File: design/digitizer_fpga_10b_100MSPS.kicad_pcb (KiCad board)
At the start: 4 copper layers, 125 x 60 mm, 284 parts, among them J1 POWER, J2 SWD_01X04, J3 DEBUG_SPI, J4 USB_B_Mini, J5 SMA, J6 JUMPER_DFS/GAIN, J7 DEBUG_FPGA_GPIO, J8 DIGILENT_JTAG_HS2_01X06, SW1 RST, SW2 PROG, U1 LM3880MF-1AA, U10 IS61WV12816EDBLL-10TLI, U11 TLV431ACDBZR, U12 AD9214, U13 XC7S15-FTGB196, U14 IS25LP064A-JKx, U2 NCP59744MN1, U3 NCP59744MN1, U4 NCP59744MN1, U5 NCP59744MN1, U6 STM32H750VBTx, U7 USBLC6-2SC6, U8 FT231XS, U9 ADA4930-1, X1 ASTX-H11-25.000MHZ-T

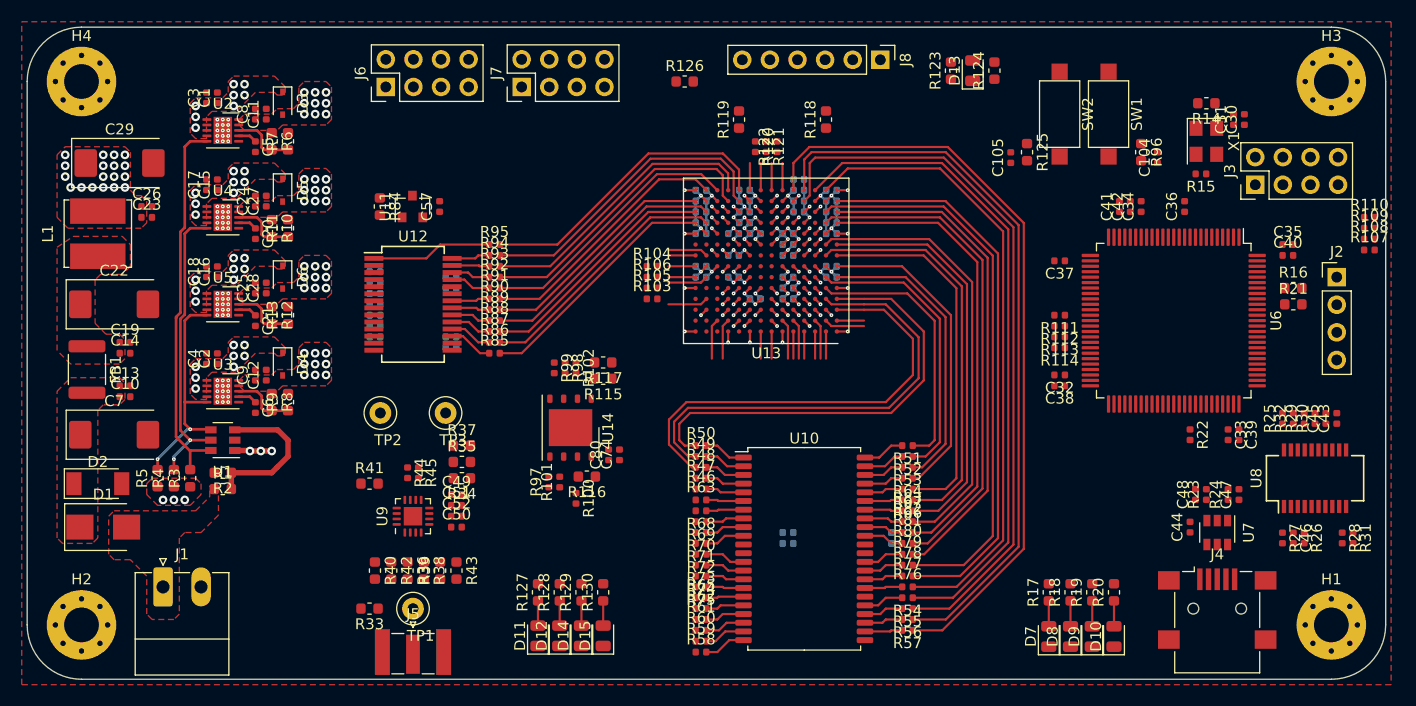
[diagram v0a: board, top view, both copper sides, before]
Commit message: Updated ADC layout
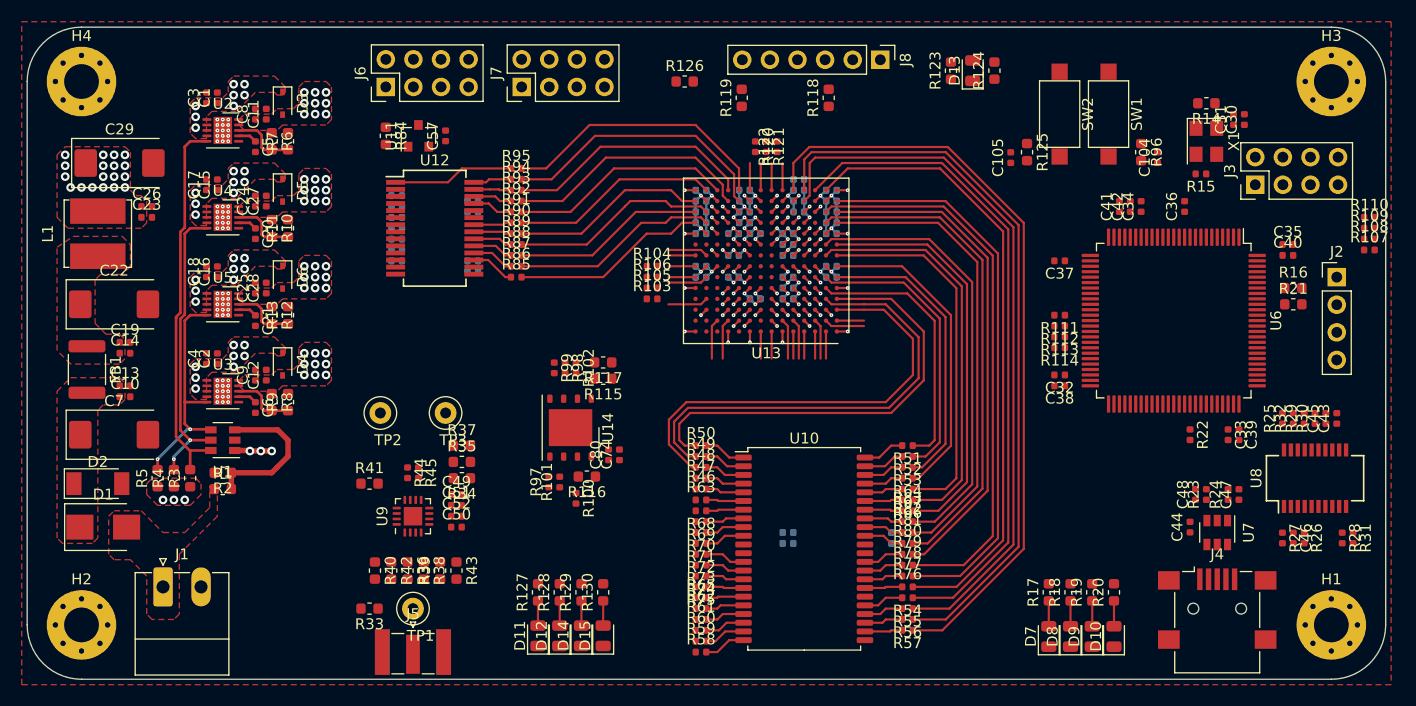
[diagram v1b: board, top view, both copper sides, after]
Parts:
- moved C58 7.28 mm to (104.0, 105.5)
- moved C59 7.28 mm to (104.0, 109.5)
- moved C60 7.28 mm to (104.0, 106.5)
- moved C61 7.28 mm to (104.0, 110.5)
- moved C62 7.28 mm to (111.0, 111.5)
- moved C63 7.28 mm to (104.0, 111.5)
- moved C64 7.28 mm to (111.0, 106.0)
- moved C65 7.28 mm to (111.0, 112.5)
- moved C66 7.28 mm to (104.0, 107.5)
- moved C67 7.28 mm to (111.0, 107.0)
- moved C68 7.28 mm to (104.0, 108.5)
- moved R85 7.28 mm to (115.0, 113.0)
- moved R86 7.28 mm to (115.0, 112.0)
- moved R87 7.28 mm to (115.0, 111.0)
- moved R88 7.28 mm to (115.0, 110.0)
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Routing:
- net /ADC_DATA5: track 24.0 -> 19.1 mm
- net /ADC_DATA2: track 22.6 -> 17.7 mm
- net /ADC_DATA1: track 24.0 -> 19.1 mm
- net /ADC_DATA0: track 23.0 -> 18.1 mm
- net /ADC_DATA7: track 27.5 -> 22.9 mm
- net /ADC_DATA3: track 23.6 -> 19.1 mm
- net /ADC_DATA6: track 25.0 -> 20.5 mm
- net /ADC_DATA4: track 22.2 -> 18.1 mm
- net /ADC_DATA8: track 26.8 -> 22.9 mm
- net /ADC_DATA9: track 28.6 -> 25.3 mm
- net /ADC_OVRNG: track 28.0 -> 25.3 mm
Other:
- net class Default: clearance 0.125 -> 0.15
- rule trace_clearance: 0.125 -> 0.15

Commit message: Added some tracks
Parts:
- moved R100 13.8 mm to (125.5, 120.5), turned to 0 degrees
- moved C74 13.2 mm to (121.5, 116.5), turned to 180 degrees
- moved C80 12.0 mm to (121.5, 117.5), turned to 180 degrees
- moved R116 12.0 mm to (123.5, 119.5), turned to -90 degrees
- moved R101 11.0 mm to (124.0, 122.0), turned to 180 degrees
- moved R97 10.7 mm to (124.0, 123.0), turned to 180 degrees
- moved R117 10.4 mm to (113.0, 118.0), turned to -90 degrees
- moved R115 9.55 mm to (114.5, 118.0), turned to -90 degrees
- moved R102 7.05 mm to (113.5, 120.5), turned to 0 degrees
- moved R98 6.00 mm to (113.5, 121.5), turned to 0 degrees
- moved U14 5.93 mm to (119.0, 121.0), turned to 0 degrees
- moved R99 5.13 mm to (113.5, 122.5), turned to 0 degrees
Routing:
- net /MCU/DEBUG_LED1: track 0.00 -> 20.5 mm
- net /MCU/DEBUG_LED2: track 0.00 -> 19.9 mm
- net /MCU/DEBUG_LED3: track 0.00 -> 19.2 mm
- net /MCU/DEBUG_LED4: track 0.00 -> 18.6 mm

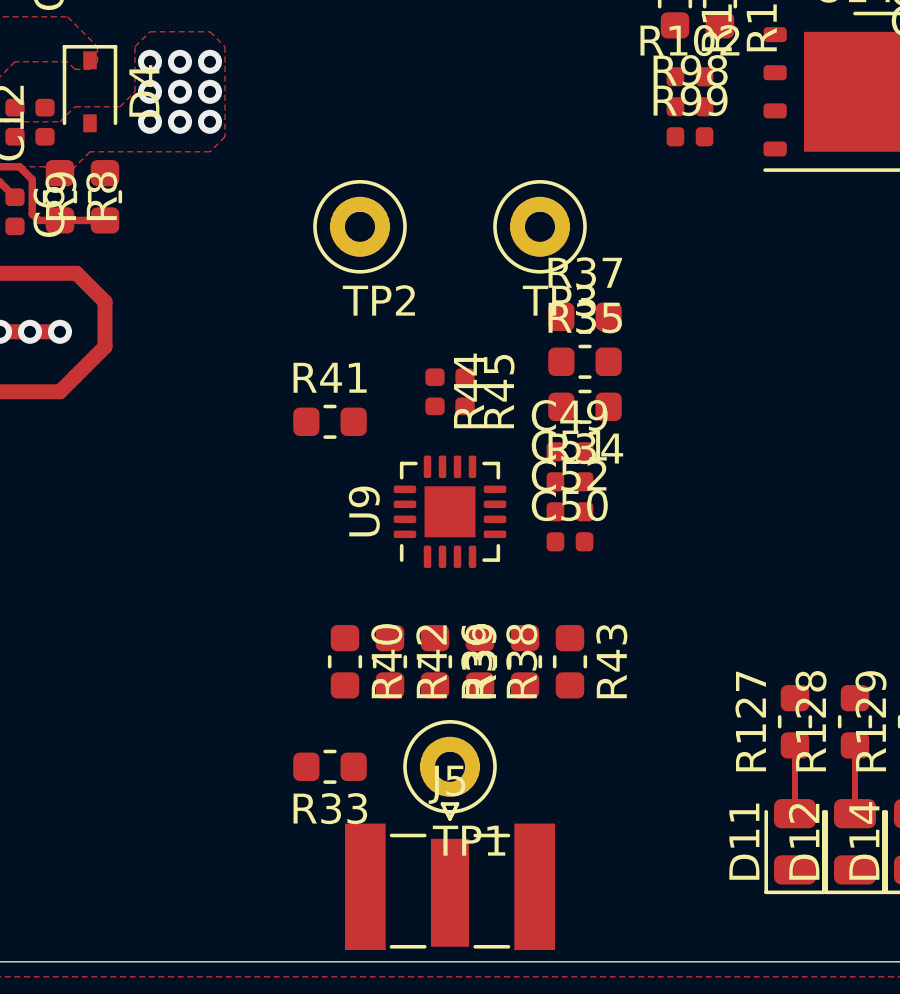
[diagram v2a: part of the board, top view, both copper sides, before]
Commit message: Changed TP footprint
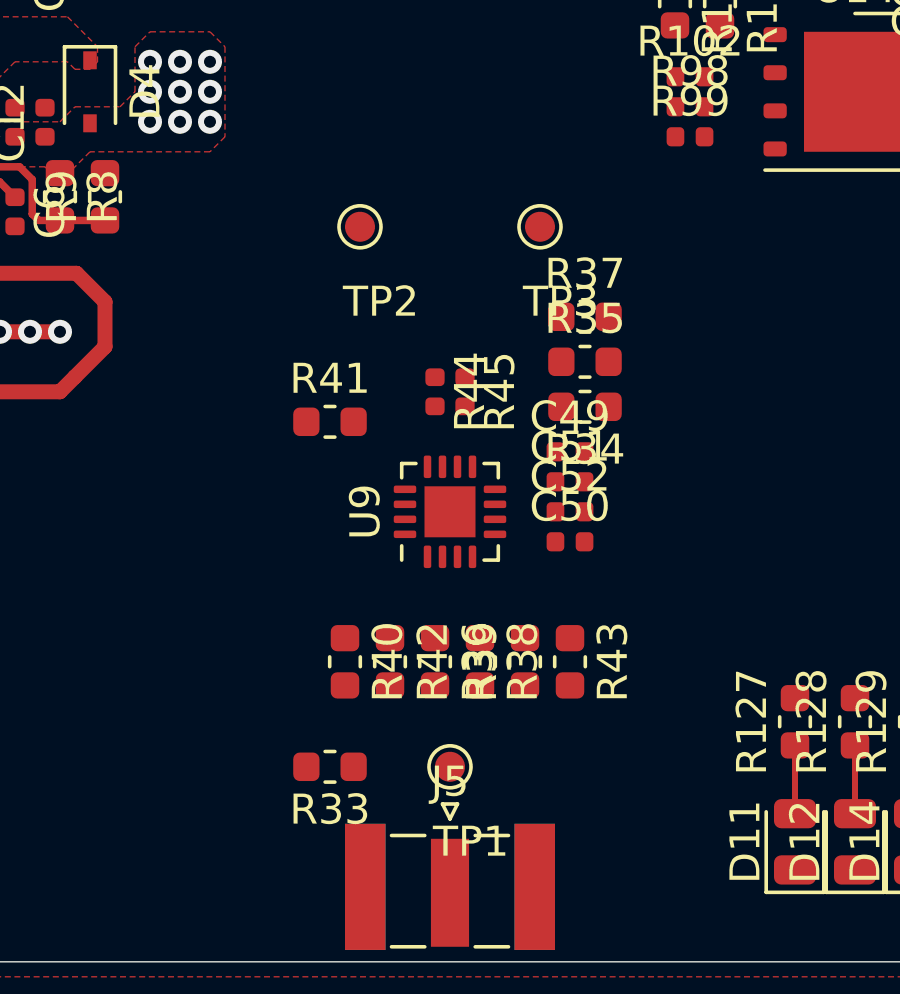
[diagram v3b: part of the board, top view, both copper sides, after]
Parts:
- TP1, TP2, TP3: footprint TestPoint:TestPoint_Loop_D2.50mm_Drill1.0mm_LowProfile -> TestPoint:TestPoint_Pad_D1.0mm
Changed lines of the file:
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@@
-(kicad_pcb (version 20200119) (host pcbnew "5.99.0-unknown-acdfeee~101~ubuntu18.04.1")
+(kicad_pcb (version 20200119) (host pcbnew "5.99.0-unknown-9ca61b5~101~ubuntu18.04.1")
   (general
     (thickness 1.628)
@@
       (dielectric_constraints yes)
     )
-    (last_trace_width 0.2)
+    (last_trace_width 0.25)
     (user_trace_width 0.2)
     (user_trace_width 0.5)
@@
     (add_net "Net-(U8-Pad8)")
   )
+  (module "TestPoint:TestPoint_Pad_D1.0mm" (layer "TOP")
+    (at 105.5 143.5)
+    (descr "SMD pad as test Point, diameter 1.0mm")
+    (tags "test point SMD pad")
+    (attr virtual)
+    (fp_text reference "TP1" (at 0.7 2.5) (layer "F.SilkS")
+      (effects (font (size 1 1) (thickness 0.15)))
+    )
+    (fp_text value "TestPoint_Probe" (at 0 -2.8) (layer "F.Fab")
+      (effects (font (size 1 1) (thickness 0.15)))
+    )
+    (fp_circle (center 0 0) (end 0 0.7) (layer "F.SilkS") (width 0.12))
+    (fp_circle (center 0 0) (end 1 0) (layer "F.CrtYd") (width 0.05))
+    (fp_text user "${REFERENCE}" (at 0.7 2.5) (layer "F.Fab")
+      (effects (font (size 1 1) (thickness 0.15)))
+    )
+    (pad "1" smd circle (at 0 0) (size 1 1) (layers "TOP" "F.Mask")
+      (net 19 "/LNA/IN") (pinfunction "1"))
+    (model "${KISYS3DMOD}/TestPoint.3dshapes/TestPoint_Loop_D2.50mm_Drill1.0mm_LowProfile.wrl"
+      (at (xyz 0 0 0))
+      (scale (xyz 1 1 1))
+      (rotate (xyz 0 0 0))
+    )
+  )
+  (module "TestPoint:TestPoint_Pad_D1.0mm" (layer "TOP")
+    (at 108.5 125.5)
+    (descr "SMD pad as test Point, diameter 1.0mm")
+    (tags "test point SMD pad")
+    (attr virtual)
+    (fp_text reference "TP3" (at 0.7 2.5) (layer "F.SilkS")
+      (effects (font (size 1 1) (thickness 0.15)))
+    )
+    (fp_text value "TestPoint_Probe" (at 0 -2.8) (layer "F.Fab")
+      (effects (font (size 1 1) (thickness 0.15)))
+    )
+    (fp_circle (center 0 0) (end 0 0.7) (layer "F.SilkS") (width 0.12))
+    (fp_circle (center 0 0) (end 1 0) (layer "F.CrtYd") (width 0.05))
+    (fp_text user "${REFERENCE}" (at 0.7 2.5) (layer "F.Fab")
+      (effects (font (size 1 1) (thickness 0.15)))
+    )
+    (pad "1" smd circle (at 0 0) (size 1 1) (layers "TOP" "F.Mask")
+      (net 39 "/OUT+") (pinfunction "1"))
+    (model "${KISYS3DMOD}/TestPoint.3dshapes/TestPoint_Loop_D2.50mm_Drill1.0mm_LowProfile.wrl"
+      (at (xyz 0 0 0))
+      (scale (xyz 1 1 1))
+      (rotate (xyz 0 0 0))
+    )
+  )
+  (module "TestPoint:TestPoint_Pad_D1.0mm" (layer "TOP")
+    (at 102.5 125.5)
+    (descr "SMD pad as test Point, diameter 1.0mm")
+    (tags "test point SMD pad")
+    (attr virtual)
+    (fp_text reference "TP2" (at 0.7 2.5) (layer "F.SilkS")
+      (effects (font (size 1 1) (thickness 0.15)))
+    )
+    (fp_text value "TestPoint_Probe" (at 0 -2.8) (layer "F.Fab")
+      (effects (font (size 1 1) (thickness 0.15)))
+    )
+    (fp_circle (center 0 0) (end 0 0.7) (layer "F.SilkS") (width 0.12))
+    (fp_circle (center 0 0) (end 1 0) (layer "F.CrtYd") (width 0.05))
+    (fp_text user "${REFERENCE}" (at 0.7 2.5) (layer "F.Fab")
+      (effects (font (size 1 1) (thickness 0.15)))
+    )
+    (pad "1" smd circle (at 0 0) (size 1 1) (layers "TOP" "F.Mask")
+      (net 38 "/OUT-") (pinfunction "1"))
+    (model "${KISYS3DMOD}/TestPoint.3dshapes/TestPoint_Loop_D2.50mm_Drill1.0mm_LowProfile.wrl"
+      (at (xyz 0 0 0))
+      (scale (xyz 1 1 1))
+      (rotate (xyz 0 0 0))
+    )
+  )
   (module "Capacitor_SMD:C_0402_1005Metric" (layer "BOT")
     (at 135 113)
@@
       (at (xyz 0 0 0))
       (scale (xyz 1 1 1))
-      (rotate (xyz 0 0 0))
-    )
-  )
-  (module "TestPoint:TestPoint_Loop_D2.50mm_Drill1.0mm_LowProfile" (layer "TOP")
-    (at 108.5 125.5)
-    (descr "low profile wire loop as test point, loop diameter 2.5mm, hole diameter 1.0mm")
-    (tags "test point wire loop bead")
-    (fp_text reference "TP3" (at 0.7 2.5) (layer "F.SilkS")
-      (effects (font (size 1 1) (thickness 0.15)))
-    )
-    (fp_text value "TestPoint_Probe" (at 0 -2.8) (layer "F.Fab")
-      (effects (font (size 1 1) (thickness 0.15)))
-    )
-    (fp_text user "${REFERENCE}" (at 0.7 2.5) (layer "F.Fab")
-      (effects (font (size 1 1) (thickness 0.15)))
-    )
-    (fp_circle (center 0 0) (end 1.5 0) (layer "F.SilkS") (width 0.12))
-    (fp_circle (center 0 0) (end 1.8 0) (layer "F.CrtYd") (width 0.05))
-    (fp_line (start 1.3 -0.2) (end -1.3 -0.2) (layer "F.Fab") (width 0.12))
-    (fp_line (start 1.3 0.2) (end 1.3 -0.2) (layer "F.Fab") (width 0.12))
-    (fp_line (start -1.3 0.2) (end 1.3 0.2) (layer "F.Fab") (width 0.12))
-    (fp_line (start -1.3 -0.2) (end -1.3 0.2) (layer "F.Fab") (width 0.12))
-    (pad "1" thru_hole circle (at 0 0) (size 2 2) (drill 1) (layers *.Cu *.Mask)
-      (net 39 "/OUT+") (pinfunction "1"))
-    (model "${KISYS3DMOD}/TestPoint.3dshapes/TestPoint_Loop_D2.50mm_Drill1.0mm_LowProfile.wrl"
-      (at (xyz 0 0 0))
-      (scale (xyz 1 1 1))
-      (rotate (xyz 0 0 0))
-    )
-  )
-  (module "TestPoint:TestPoint_Loop_D2.50mm_Drill1.0mm_LowProfile" (layer "TOP")
-    (at 102.5 125.5)
-    (descr "low profile wire loop as test point, loop diameter 2.5mm, hole diameter 1.0mm")
-    (tags "test point wire loop bead")
-    (fp_text reference "TP2" (at 0.7 2.5) (layer "F.SilkS")
-      (effects (font (size 1 1) (thickness 0.15)))
-    )
-    (fp_text value "TestPoint_Probe" (at 0 -2.8) (layer "F.Fab")
-      (effects (font (size 1 1) (thickness 0.15)))
-    )
-    (fp_text user "${REFERENCE}" (at 0.7 2.5) (layer "F.Fab")
-      (effects (font (size 1 1) (thickness 0.15)))
-    )
-    (fp_circle (center 0 0) (end 1.5 0) (layer "F.SilkS") (width 0.12))
-    (fp_circle (center 0 0) (end 1.8 0) (layer "F.CrtYd") (width 0.05))
-    (fp_line (start 1.3 -0.2) (end -1.3 -0.2) (layer "F.Fab") (width 0.12))
-    (fp_line (start 1.3 0.2) (end 1.3 -0.2) (layer "F.Fab") (width 0.12))
-    (fp_line (start -1.3 0.2) (end 1.3 0.2) (layer "F.Fab") (width 0.12))
-    (fp_line (start -1.3 -0.2) (end -1.3 0.2) (layer "F.Fab") (width 0.12))
-    (pad "1" thru_hole circle (at 0 0) (size 2 2) (drill 1) (layers *.Cu *.Mask)
-      (net 38 "/OUT-") (pinfunction "1"))
-    (model "${KISYS3DMOD}/TestPoint.3dshapes/TestPoint_Loop_D2.50mm_Drill1.0mm_LowProfile.wrl"
-      (at (xyz 0 0 0))
-      (scale (xyz 1 1 1))
-      (rotate (xyz 0 0 0))
-    )
-  )
-  (module "TestPoint:TestPoint_Loop_D2.50mm_Drill1.0mm_LowProfile" (layer "TOP")
-    (at 105.5 143.5)
-    (descr "low profile wire loop as test point, loop diameter 2.5mm, hole diameter 1.0mm")
-    (tags "test point wire loop bead")
-    (fp_text reference "TP1" (at 0.7 2.5) (layer "F.SilkS")
-      (effects (font (size 1 1) (thickness 0.15)))
-    )
-    (fp_text value "TestPoint_Probe" (at 0 -2.8) (layer "F.Fab")
-      (effects (font (size 1 1) (thickness 0.15)))
-    )
-    (fp_text user "${REFERENCE}" (at 0.7 2.5) (layer "F.Fab")
-      (effects (font (size 1 1) (thickness 0.15)))
-    )
-    (fp_circle (center 0 0) (end 1.5 0) (layer "F.SilkS") (width 0.12))
-    (fp_circle (center 0 0) (end 1.8 0) (layer "F.CrtYd") (width 0.05))
-    (fp_line (start 1.3 -0.2) (end -1.3 -0.2) (layer "F.Fab") (width 0.12))
-    (fp_line (start 1.3 0.2) (end 1.3 -0.2) (layer "F.Fab") (width 0.12))
-    (fp_line (start -1.3 0.2) (end 1.3 0.2) (layer "F.Fab") (width 0.12))
-    (fp_line (start -1.3 -0.2) (end -1.3 0.2) (layer "F.Fab") (width 0.12))
-    (pad "1" thru_hole circle (at 0 0) (size 2 2) (drill 1) (layers *.Cu *.Mask)
-      (net 19 "/LNA/IN") (pinfunction "1"))
-    (model "${KISYS3DMOD}/TestPoint.3dshapes/TestPoint_Loop_D2.50mm_Drill1.0mm_LowProfile.wrl"
-      (at (xyz 0 0 0))
-      (scale (xyz 1 1 1))
